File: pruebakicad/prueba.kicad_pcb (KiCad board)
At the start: 2 copper layers, 94 x 45 mm, 37 parts, among them J1 Conn_01x08_RC522, J2 Conn_01x04_MountingPin, J3 Conn_01x03, J4 Conn_2Rows-15Pins, J5 Conn_01x04, J6 Conn_01x02, Q1 BSS138, Q2 BSS138, U1 TLV1117-33, U2 TLV1117-50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

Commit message: full
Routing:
- net +5V: track 191.2 -> 190.7 mm

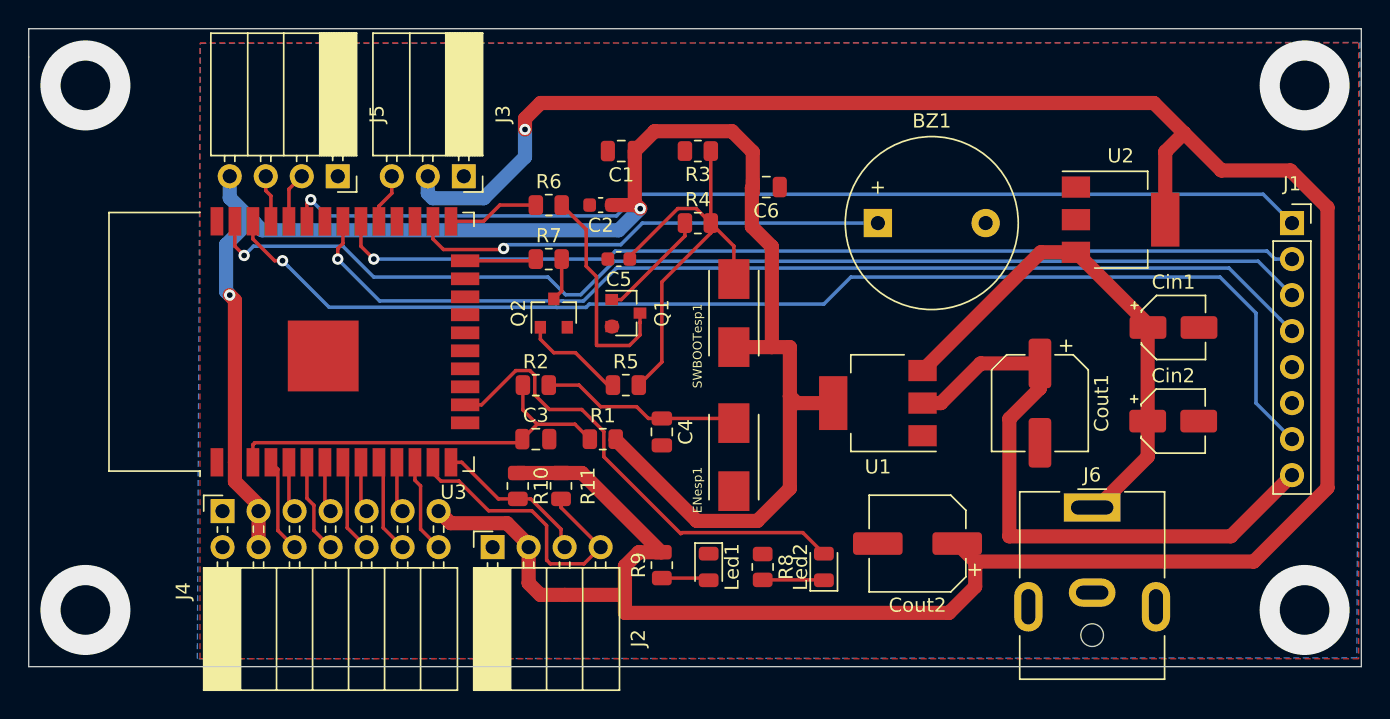
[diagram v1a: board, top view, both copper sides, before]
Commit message: huecos gnd
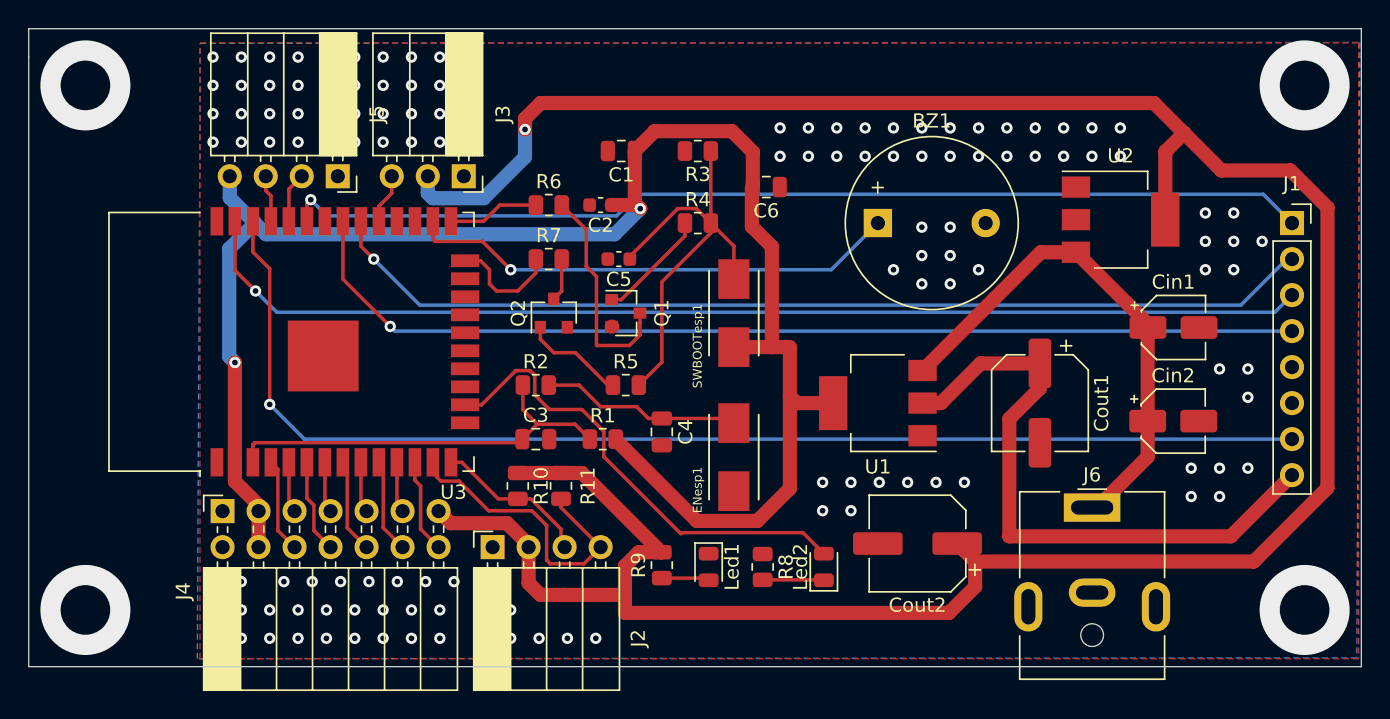
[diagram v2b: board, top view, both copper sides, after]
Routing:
- net /esp32-wroom/IO2: track 5.03 -> 7.96 mm
- net /SCK: track 68.3 -> 70.5 mm
- net /MISO: track 74.2 -> 72.5 mm
- net /BUZ: track 33.7 -> 34.9 mm
- net /RST: track 85.9 -> 86.5 mm
- net GND: vias 0 -> 132
